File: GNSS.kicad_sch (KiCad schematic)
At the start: 11 parts, among them U14 SAM-M10Q-00B

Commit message: Chore: push new design
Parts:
- removed LED2: QBLP617-AG1, PCM_JLCPCB:D_0603, symbol PCM_JLCPCB-Diodes:LED,0603,Red
- removed R36: 1kΩ, PCM_JLCPCB:R_0603, symbol PCM_JLCPCB-Resistors:0402,1kΩ
- C51: footprint PCM_JLCPCB:C_0402 -> PCM_JLCPCB:C_0603
- D6: Ratings 0.5A/40V -> 0.5A/20V

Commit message: Special version
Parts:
- C51: Digikey Parts (none) -> CL10B105KO8NNNC
- R11, R34: Digikey Parts (none) -> RC0603JR-07470RL
- R18: Digikey Parts (none) -> RC0603JR-071KL
- R20: Digikey Parts (none) -> RMCF0603JT3K30
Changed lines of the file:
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@@
+			)
+		)
+		(property "Digikey Parts" ""
+			(at 92.71 92.71 0)
+			(effects
+				(font
+					(size 1.27 1.27)
+				)
 			)
 		)
@@
 			)
 		)
+		(property "Digikey Parts" "RC0603JR-071KL"
+			(at 30.48 93.98 0)
+			(effects
+				(font
+					(size 1.27 1.27)
+				)
+			)
+		)
 		(pin "1"
 		)
@@
 			)
 		)
+		(property "Digikey Parts" "RMCF0603JT3K30"
+			(at 92.71 100.33 0)
+			(effects
+				(font
+					(size 1.27 1.27)
+				)
+			)
+		)
 		(pin "1"
 		)
@@
 			)
 		)
+		(property "Digikey Parts" "RC0603JR-07470RL"
+			(at 100.33 49.53 0)
+			(effects
+				(font
+					(size 1.27 1.27)
+				)
+			)
+		)
 		(pin "1"
 		)
@@
 			)
 		)
+		(property "Digikey Parts" "CL10B105KO8NNNC"
+			(at 123.19 119.38 0)
+			(effects
+				(font
+					(size 1.27 1.27)
+				)
+			)
+		)
 		(pin "2"
 		)
@@
 			)
 		)
+		(property "Digikey Parts" "RC0603JR-07470RL"
+			(at 100.33 46.99 0)
+			(effects
+				(font
+					(size 1.27 1.27)
+				)
+			)
+		)
 		(pin "1"
 		)
@@
 			)
 		)
+		(property "Digikey Parts" ""
+			(at 30.48 102.87 0)
+			(effects
+				(font
+					(size 1.27 1.27)
+				)
+			)
+		)
 		(pin "2"
 		)
@@
 			)
 		)
+		(property "Digikey Parts" ""
+			(at 67.31 43.18 0)
+			(effects
+				(font
+					(size 1.27 1.27)
+				)
+			)
+		)
 		(pin "6"
 		)
@@
 			(at 92.71 121.92 0)
 			(effects
+				(font
+					(size 1.27 1.27)
+				)
+			)
+		)
+		(property "Digikey Parts" ""
+			(at 92.71 121.92 0)
+			(effects

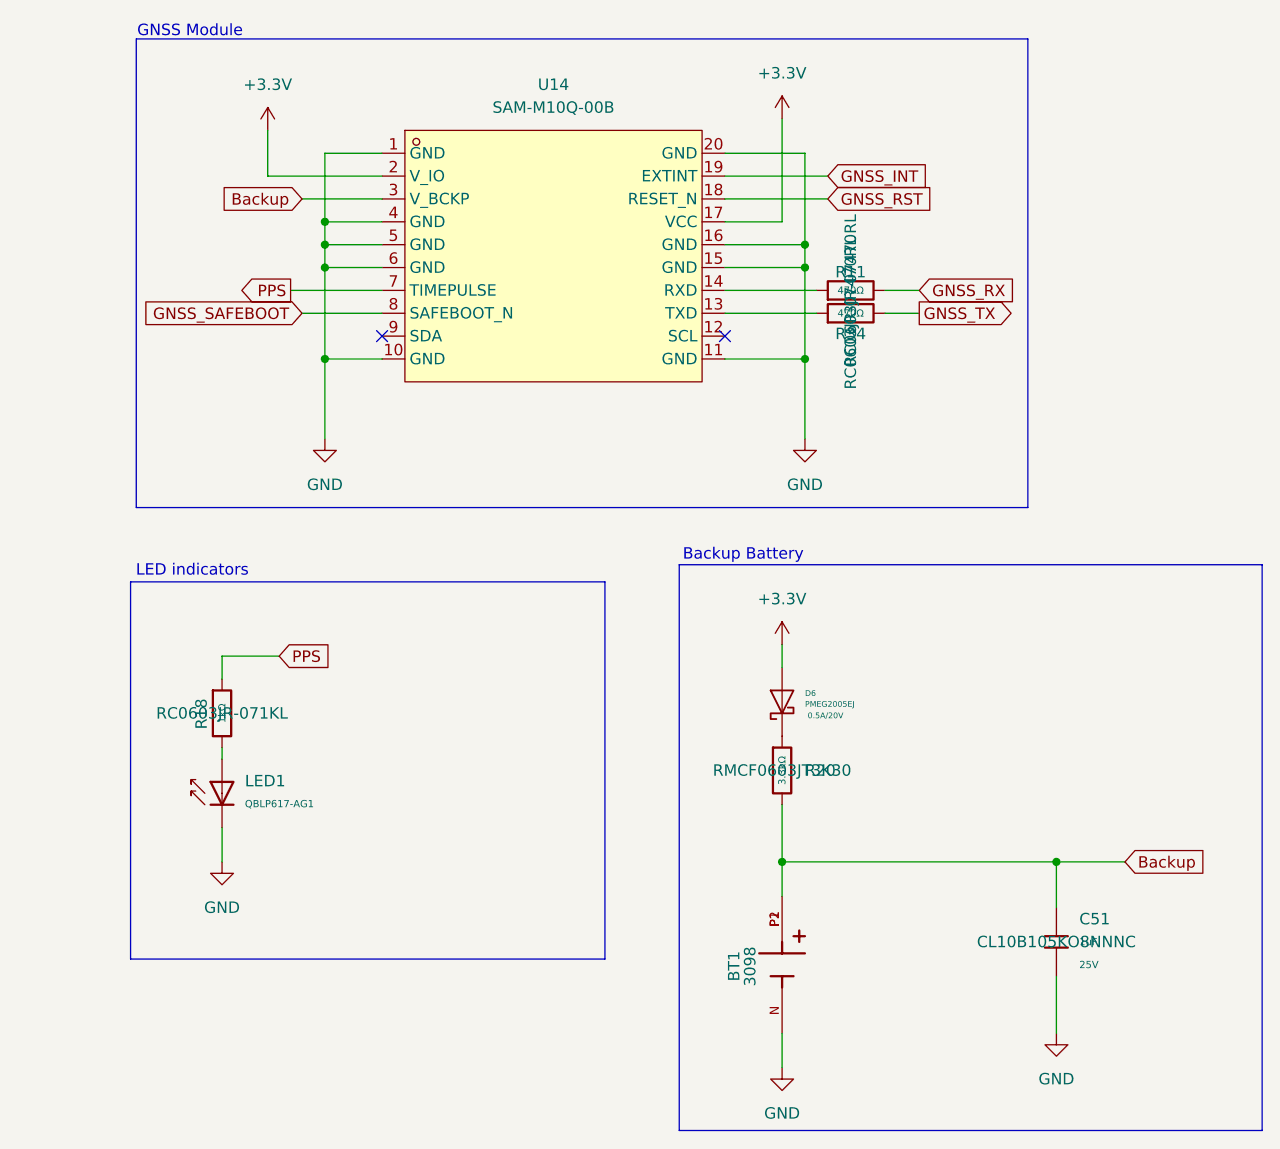
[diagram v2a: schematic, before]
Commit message: Chore: Add Digikey Part to symbols
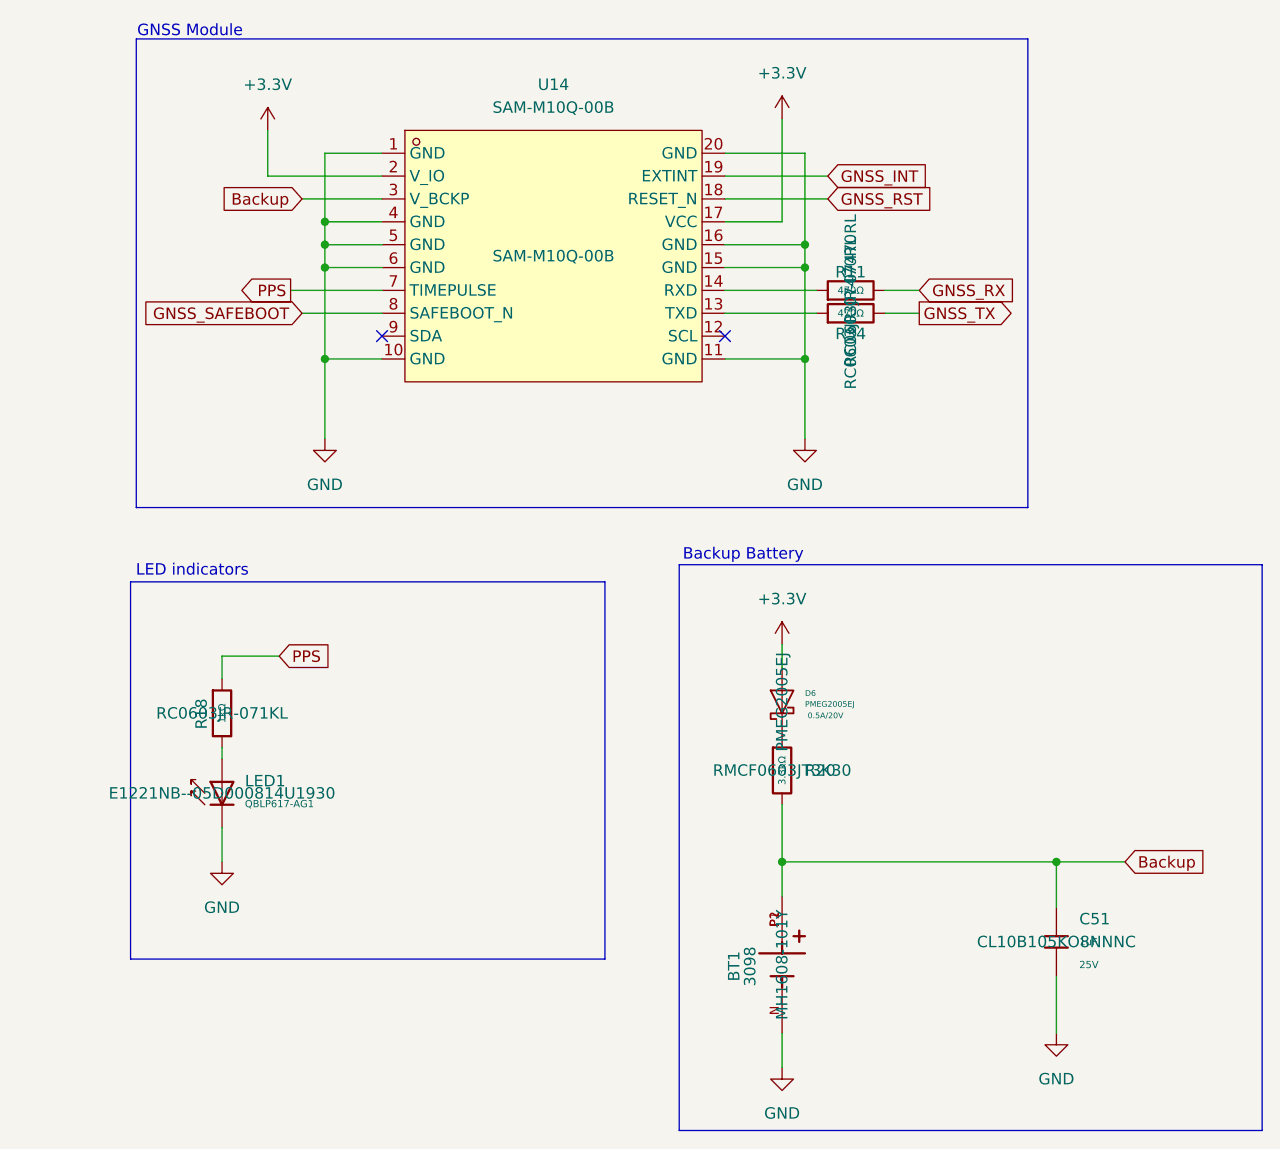
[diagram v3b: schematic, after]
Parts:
- BT1: Digikey Parts (none) -> MH1608-101Y
- D6: Digikey Parts (none) -> PMEG2005EJ
- LED1: Digikey Parts (none) -> E1221NB--05D000814U1930
- U14: Digikey Parts (none) -> SAM-M10Q-00B
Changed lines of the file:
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@@
 			)
 		)
-		(property "Digikey Parts" ""
+		(property "Digikey Parts" "PMEG2005EJ"
 			(at 92.71 92.71 0)
 			(effects
@@
 			)
 		)
-		(property "Digikey Parts" ""
+		(property "Digikey Parts" "E1221NB--05D000814U1930"
 			(at 30.48 102.87 0)
 			(effects
@@
 			)
 		)
-		(property "Digikey Parts" ""
+		(property "Digikey Parts" "SAM-M10Q-00B"
 			(at 67.31 43.18 0)
 			(effects
@@
 			)
 		)
-		(property "Digikey Parts" ""
+		(property "Digikey Parts" "MH1608-101Y"
 			(at 92.71 121.92 0)
 			(effects

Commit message: Feat: Minor improvement
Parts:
- removed R18: 1kΩ, PCM_JLCPCB:R_0603, symbol PCM_JLCPCB-Resistors:0402,1kΩ
- added R18: 470Ω, PCM_JLCPCB:R_0603, symbol PCM_JLCPCB-Resistors:0402,470Ω
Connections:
- net PPS: now also R18.1
- net at LED1.2: now also R18.2

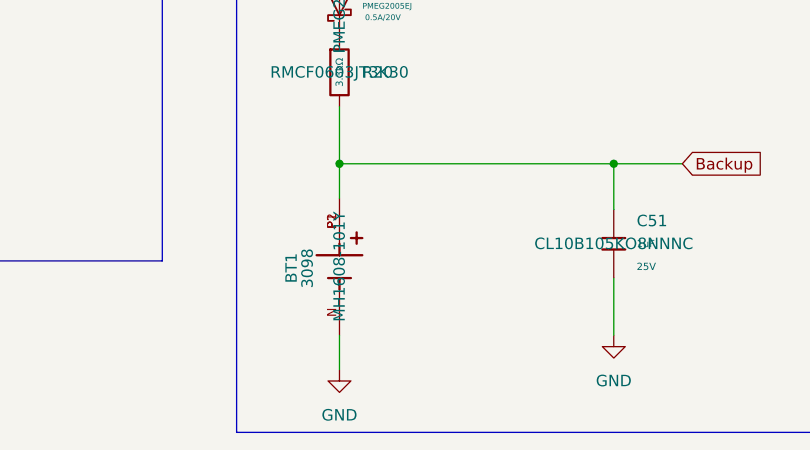
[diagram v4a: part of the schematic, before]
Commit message: Added silkscreen + Changed gps vbackup
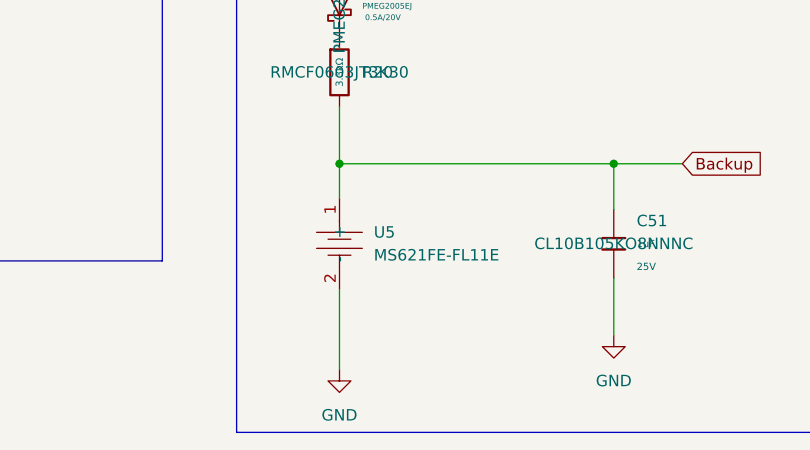
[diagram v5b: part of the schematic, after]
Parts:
- removed BT1: 3098, GNSS:BAT_3098, symbol Battery3V_holder:3098
- added U5: MS621FE-FL11E, EasyEDA:BAT-SMD_FL11E, symbol EasyEDA:MS621FE-FL11E
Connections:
- net Backup: now also U5.1 (+)
- net GND: now also U5.2 (-)
